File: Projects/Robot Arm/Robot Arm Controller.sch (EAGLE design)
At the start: 64 parts, among them IC1 U_FTDICHIP_FT232RL, J1 ICSP HEADER, J2 SERVO PWR, J3 STEPPER, J4 J_MOLEX_502386, P1 P_USB_MINIUX60A-MB-5ST, P2 +12V INPUT, U1 UA78M05CDCY, U2 TPS71550DCKR, U3 U_ATMEGA328P-AU, U4 U_5VSWITCHER_TL2575-05IKTTR, U5 A4988ALT1, U6 U_OPAMP_MCP6001T-E/OT, Y1 CSTCE16M0V13

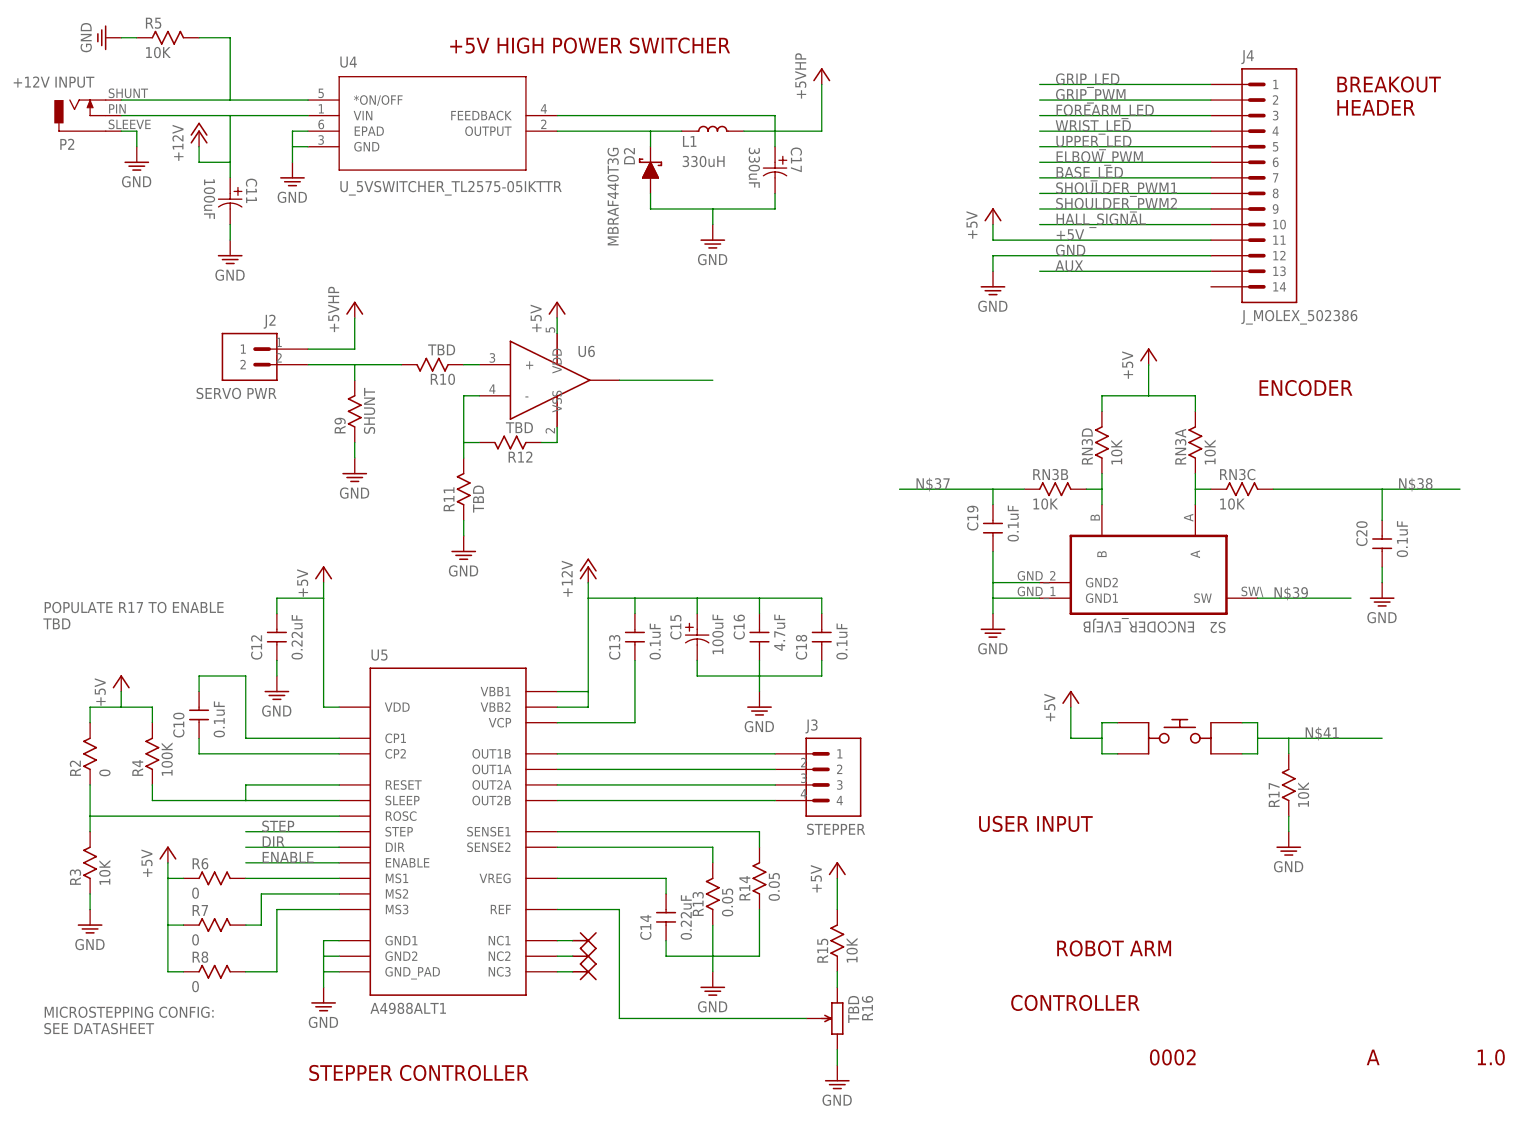
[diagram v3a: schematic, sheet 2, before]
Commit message: updated robot arm schematic to rev 1.1
- revisions to library
- 3A 5V support
- changed i/o position
- added component values
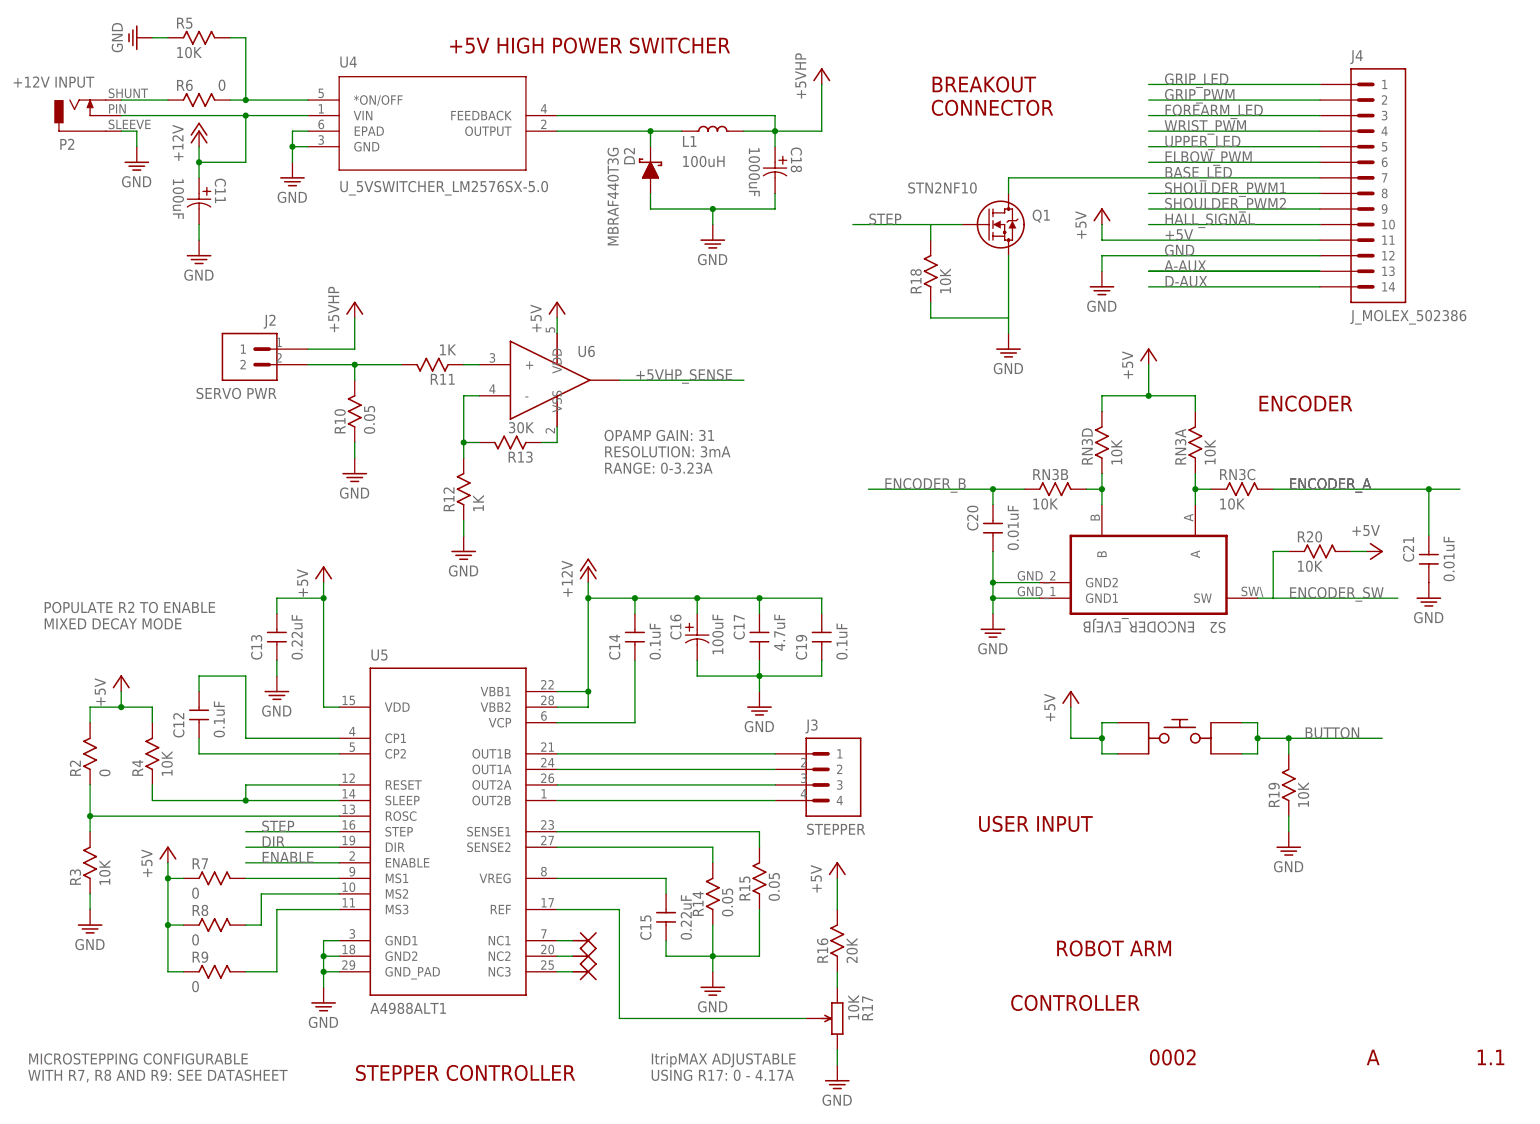
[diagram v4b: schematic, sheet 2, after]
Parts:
- added C21: 0.01uF, devon:C_CAPACITORC0805
- added Q1: STN2NF10, devon:Q_MOSFET_STN2NF10
- added R18, R19, R20: 10K, devon:R_RESISTOR0805
- C10: value 0.1uF -> 4.7uF
- C12, C14: value 0.22uF -> 0.1uF
- C13: value 0.1uF -> 0.22uF
- C15: value 100uF -> 0.22uF; device devon:C_CAPACITOR_ALUMINUM_PCAP_SVP_F12 -> devon:C_CAPACITORC0805
- C16: value 4.7uF -> 100uF; device devon:C_CAPACITORC1206 -> devon:C_CAPACITOR_ALUMINUM_PCAP_SVP_F12
- C17: value 330uF -> 4.7uF; device devon:C_CAPACITOR_ALUMINUM_PCAP_SVP_F12 -> devon:C_CAPACITORC1206
- C18: value 0.1uF -> 1000uF; device devon:C_CAPACITORC0805 -> devon:C_CAPACITOR_ALUMINUM_PCAP_SVP_F12
- C20: value 0.1uF -> 0.01uF
- C9: value 4.7uF -> 0.1uF
- L1: value 330uH -> 100uH; device devon:L_INDUCTOR_CLF12577NI-D -> devon:L_INDUCTOR_PA4344.104NLT
- R10: value TBD -> 0.05; device devon:R_RESISTOR0805 -> devon:R_RESISTOR1206
- R11, R12: value TBD -> 1K
- R13: value 0.05 -> 30K; device devon:R_RESISTOR1206 -> devon:R_RESISTOR0805
- R15: value 10K -> 0.05; device devon:R_RESISTOR0805 -> devon:R_RESISTOR1206
- R16: value TBD -> 20K; device devon:R_POT_EVM-2WSX80B14 -> devon:R_RESISTOR0805
- R17: device devon:R_RESISTOR0805 -> devon:R_POT_EVM-2WSX80B14
- R4: value 100K -> 10K
- R9: value SHUNT -> 0; device devon:R_RESISTOR1206 -> devon:R_RESISTOR0805
- RN2: value 10K -> 1K
- U4: value U_5VSWITCHER_TL2575-05IKTTR -> U_5VSWITCHER_LM2576SX-5.0; device devon:U_5VSWITCHER_TL2575-05IKTTR -> devon:U_5VSWITCHER_LM2576SX-5.0/NOPB
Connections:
- removed net A0: U3.PC0(ADC0)
- removed net A1: U3.PC1(ADC1)
- removed net A2: U3.PC2(ADC2)
- removed net A3: U3.PC3(ADC3)
- removed net A4: U3.PC4(ADC4)
- removed net A5: U3.PC5(ADC5)
- removed net A6: U3.ADC6
- removed net A7: U3.ADC7
- removed net AUX: J4.13
- removed net D10: U3.PB2
- removed net D2: U3.PD2
- removed net D3: U3.PD3
- removed net D4: U3.PD4
- removed net D5: U3.PD5
- removed net D6: U3.PD6
- removed net D7: U3.PD7
- removed net D8: U3.PB0
- removed net D9: U3.PB1
- removed net N$37: C19.2, RN3B.1
- removed net N$38: C20.2, RN3C.2
- removed net N$39: S2.SW
- removed net N$41: R17.2, S3.3, S3.4
- removed net N$49: U6.VOUT
- removed net WRIST_LED: J4.4
- new net +5VHP_SENSE: U3.ADC6, U6.VOUT
- new net A-AUX: J4.13, U3.ADC7
- new net BUTTON: R19.2, S3.3, S3.4, U3.PC3(ADC3)
- new net D-AUX: J4.14, U3.PC0(ADC0)
- new net ENCODER_A: C21.2, RN3C.2, U3.PD2(D2)
- new net ENCODER_B: C20.2, RN3B.1, U3.PC5(ADC5)
- new net ENCODER_SW: R20.1, S2.SW, U3.PC4(ADC4)
- new net N$66: P1.2
- new net N$67: P2.SHUNT, R6.1
- new net STAT: RN1A.2, U3.PB5(D13)
- new net WRIST_PWM: J4.4, U3.PB2(D10)
- net +12V: now also C14.1, C16.11, C17.2, C19.1; no longer C13.1, C15.11, C16.2, C18.1
- net +5V: now also C10.1, C13.1, C18.11, C7.1, LED3.A, LED4.A, R16.2, R20.2, R9.1; no longer C12.1, C17.11, C6.1, C9.1, LED3.C, LED4.C, R15.2, R6.1
- net BASE_LED: now also Q1.2
- net D11/MOSI: no longer U3.PB3
- net D12/MISO: no longer U3.PB4
- net D13/SCK: no longer RN1A.2, U3.PB5
- net DIR: now also U3.PD3(D3)
- net ELBOW_PWM: now also U3.PB1(D9)
- net ENABLE: now also U3.PC2(ADC2)
- net FOREARM_LED: now also U3.PB0(D8)
- net GND: now also C10.2, C13.2, C15.2, C16.22, C17.1, C18.22, C19.2, C21.1, C8.2, Q1.3, R10.1, R12.1, R15.1, R17.3, R18.1, R19.1; no longer C12.2, C14.2, C15.22, C16.1, C17.22, C18.2, C19.1, C9.2, R11.1, R13.1, R16.3, R17.1, R9.1
- net GRIP_LED: now also U3.PB4(D12)
- net GRIP_PWM: now also U3.PB3(D11)
- net HALL_SIGNAL: now also U3.PC1(ADC1)
- net N$11: now also C6.1
- net N$20: now also U3.PD0(RX); no longer U3.PD0
- net N$27: now also C9.2; no longer C8.2
- net N$30: now also LED3.C; no longer LED3.A
- net N$31: now also LED4.C; no longer LED4.A
- net N$35: now also R6.2; no longer P2.SHUNT
- net N$42: now also R13.1; no longer R12.1
- net N$43: now also R11.1; no longer R10.1
- net N$44: now also R13.2; no longer R11.2
- net N$45: now also R11.2; no longer R9.2
- net N$50: now also C15.1; no longer C14.1
- net N$51: now also R14.2; no longer R13.2
- net N$52: now also R17.1; no longer R15.1
- net N$53: now also R15.2; no longer R14.2
- net N$54: now also R17.2; no longer R16.2
- net N$58: now also C14.2; no longer C13.2
- net N$59: now also C12.2; no longer C10.2
- net N$6: now also C8.1; no longer C7.1
- net N$60: now also C12.1; no longer C10.1
- net N$61: now also R8.2; no longer R7.2
- net N$62: now also R7.2; no longer R6.2
- net N$63: now also R9.2; no longer R8.2
- net N$9: now also U3.PD1(TX); no longer U3.PD1
- net RESET: now also C9.1; no longer C8.1
- net SHOULDER_PWM1: now also U3.PD5(D5)
- net SHOULDER_PWM2: now also U3.PD6(D6)
- net STEP: now also Q1.1, R18.2, U3.PD4(D4)
- net UPPER_LED: now also U3.PD7(D7)
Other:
- note added: "1.1"
- note added: "BREAKOUT CONNECTOR"
- note added: "ItripMAX ADJUSTABLE USING R17: 0 - 4.17A"
- note added: "MICROSTEPPING CONFIGURABLE WITH R7, R8 AND R9: SEE DATASHEET"
- note added: "OPAMP GAIN: 31 RESOLUTION: 3mA RANGE: 0-3.23A"
- note added: "POPULATE R2 TO ENABLE MIXED DECAY MODE"
- note removed: "1.0"
- note removed: "BREAKOUT HEADER"
- note removed: "MICROSTEPPING CONFIG: SEE DATASHEET"
- note removed: "POPULATE R17 TO ENABLE TBD"
- moved on the sheet: C11, C12, C13, C14, C19, C20, C4, C6, C7, C8, C9, J4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

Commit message: Started placing components
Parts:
- added C22: 0.1uF, devon:C_CAPACITORC0805
- C11, C16: device devon:C_CAPACITOR_ALUMINUM_PCAP_SVP_F12 -> devon:C_100UF_ALUMINUM_APXG160ARA101ME61G
- C18: device devon:C_CAPACITOR_ALUMINUM_PCAP_SVP_F12 -> devon:C_1000UF_ALUMINUM_APXG160ARA102MJA0G
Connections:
- net A-AUX renamed A_AUX
- net D-AUX renamed D_AUX
- net +12V: now also C11.+, C16.+, C22.1; no longer C11.11, C16.11
- net +5V: now also C18.+; no longer C18.11
- net GND: now also C11.-, C16.-, C18.-, C22.2; no longer C11.22, C16.22, C18.22
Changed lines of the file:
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@@
 <part name="ZZ17" library="devon" deviceset="ZZ_NC" device=""/>
 <part name="U4" library="devon" deviceset="U_5VSWITCHER_LM2576SX-5.0/NOPB" device="" value="U_5VSWITCHER_LM2576SX-5.0"/>
-<part name="C11" library="devon" deviceset="C_CAPACITOR_ALUMINUM_PCAP_SVP_F12" device="" value="100uF"/>
-<part name="C18" library="devon" deviceset="C_CAPACITOR_ALUMINUM_PCAP_SVP_F12" device="" value="1000uF"/>
+<part name="C11" library="devon" deviceset="C_100UF_ALUMINUM_APXG160ARA101ME61G" device="" value="100uF"/>
+<part name="C18" library="devon" deviceset="C_1000UF_ALUMINUM_APXG160ARA102MJA0G" device="" value="1000uF"/>
 <part name="L1" library="devon" deviceset="L_INDUCTOR_PA4344.104NLT" device="" value="100uH"/>
 <part name="P2" library="devon" deviceset="P_BARREL_2.1MM" device="" value="+12V INPUT"/>
@@
 <part name="R14" library="devon" deviceset="R_RESISTOR" device="1206" value="0.05"/>
 <part name="R15" library="devon" deviceset="R_RESISTOR" device="1206" value="0.05"/>
-<part name="C16" library="devon" deviceset="C_CAPACITOR_ALUMINUM_PCAP_SVP_F12" device="" value="100uF"/>
+<part name="C16" library="devon" deviceset="C_100UF_ALUMINUM_APXG160ARA101ME61G" device="" value="100uF"/>
 <part name="C17" library="devon" deviceset="C_CAPACITOR" device="C1206" value="4.7uF"/>
 <part name="C15" library="devon" deviceset="C_CAPACITOR" device="C0805" value="0.22uF"/>
@@
 <part name="R20" library="devon" deviceset="R_RESISTOR" device="0805" value="10K"/>
 <part name="P+24" library="devon-supply" deviceset="+5V" device=""/>
+<part name="C22" library="devon" deviceset="C_CAPACITOR" device="C0805" value="0.1uF"/>
 </parts>
 <sheets>
@@
 <segment>
 <pinref part="U3" gate="A" pin="ADC6"/>
-<wire x1="142.24" y1="-40.64" x2="127" y2="-40.64" width="0.1524" layer="91"/>
-<label x="129.54" y="-40.64" size="1.778" layer="95"/>
-</segment>
-</net>
-<net name="A-AUX" class="0">
-<segment>
-<pinref part="U3" gate="A" pin="ADC7"/>
-<wire x1="142.24" y1="-43.18" x2="127" y2="-43.18" width="0.1524" layer="91"/>
-<label x="129.54" y="-43.18" size="1.778" layer="95"/>
+<wire x1="142.24" y1="-40.64" x2="119.38" y2="-40.64" width="0.1524" layer="91"/>
+<label x="121.92" y="-40.64" size="1.778" layer="95"/>
 </segment>
 </net>
@@
 </segment>
 </net>
-<net name="D-AUX" class="0">
-<segment>
-<pinref part="U3" gate="A" pin="PC0(ADC0)"/>
-<wire x1="185.42" y1="-30.48" x2="200.66" y2="-30.48" width="0.1524" layer="91"/>
-<label x="187.96" y="-30.48" size="1.778" layer="95"/>
-</segment>
-</net>
 <net name="HALL_SIGNAL" class="0">
 <segment>
@@
 <wire x1="142.24" y1="-63.5" x2="119.38" y2="-63.5" width="0.1524" layer="91"/>
 <label x="121.92" y="-63.5" size="1.778" layer="95"/>
+</segment>
+</net>
+<net name="A_AUX" class="0">
+<segment>
+<pinref part="U3" gate="A" pin="ADC7"/>
+<wire x1="142.24" y1="-43.18" x2="119.38" y2="-43.18" width="0.1524" layer="91"/>
+<label x="121.92" y="-43.18" size="1.778" layer="95"/>
+</segment>
+</net>
+<net name="D_AUX" class="0">
+<segment>
+<pinref part="U3" gate="A" pin="PC0(ADC0)"/>
+<wire x1="185.42" y1="-30.48" x2="200.66" y2="-30.48" width="0.1524" layer="91"/>
+<label x="187.96" y="-30.48" size="1.778" layer="95"/>
 </segment>
 </net>
@@
 <instance part="R20" gate="A" x="215.9" y="-91.44"/>
 <instance part="P+24" gate="1" x="226.06" y="-91.44" rot="R270"/>
+<instance part="C22" gate="G$1" x="144.78" y="-109.22" rot="R90"/>
 </instances>
 <busses>
@@
 </segment>
 <segment>
-<pinref part="C11" gate="A" pin="22"/>
+<pinref part="C11" gate="A" pin="-"/>
 <wire x1="33.02" y1="-38.1" x2="33.02" y2="-40.64" width="0.1524" layer="91"/>
 <pinref part="GND19" gate="1" pin="GND"/>
@@
 <pinref part="D2" gate="G$1" pin="A"/>
 <wire x1="106.68" y1="-33.02" x2="106.68" y2="-35.56" width="0.1524" layer="91"/>
-<pinref part="C18" gate="A" pin="22"/>
+<pinref part="C18" gate="A" pin="-"/>
 <wire x1="106.68" y1="-35.56" x2="116.84" y2="-35.56" width="0.1524" layer="91"/>
 <wire x1="116.84" y1="-35.56" x2="127" y2="-35.56" width="0.1524" layer="91"/>
@@
 <wire x1="134.62" y1="-111.76" x2="124.46" y2="-111.76" width="0.1524" layer="91"/>
 <wire x1="124.46" y1="-111.76" x2="124.46" y2="-109.22" width="0.1524" layer="91"/>
-<pinref part="C16" gate="A" pin="22"/>
+<pinref part="C16" gate="A" pin="-"/>
 <wire x1="124.46" y1="-111.76" x2="114.3" y2="-111.76" width="0.1524" layer="91"/>
 <wire x1="114.3" y1="-111.76" x2="114.3" y2="-109.22" width="0.1524" layer="91"/>
@@
 <pinref part="GND27" gate="1" pin="GND"/>
 <junction x="124.46" y="-111.76"/>
+<pinref part="C22" gate="G$1" pin="2"/>
+<wire x1="144.78" y1="-109.22" x2="144.78" y2="-111.76" width="0.1524" layer="91"/>
+<wire x1="144.78" y1="-111.76" x2="134.62" y2="-111.76" width="0.1524" layer="91"/>
+<junction x="134.62" y="-111.76"/>
 </segment>
 <segment>
@@
 <wire x1="40.64" y1="-27.94" x2="40.64" y2="-20.32" width="0.1524" layer="91"/>
 <wire x1="33.02" y1="-27.94" x2="40.64" y2="-27.94" width="0.1524" layer="91"/>
-<pinref part="C11" gate="A" pin="11"/>
+<pinref part="C11" gate="A" pin="+"/>
 <wire x1="33.02" y1="-27.94" x2="33.02" y2="-30.48" width="0.1524" layer="91"/>
 <junction x="40.64" y="-20.32"/>
@@
 <wire x1="114.3" y1="-99.06" x2="124.46" y2="-99.06" width="0.1524" layer="91"/>
 <wire x1="124.46" y1="-99.06" x2="124.46" y2="-101.6" width="0.1524" layer="91"/>
-<pinref part="C16" gate="A" pin="11"/>
+<pinref part="C16" gate="A" pin="+"/>
 <pinref part="C17" gate="G$1" pin="2"/>
 <pinref part="C19" gate="G$1" pin="1"/>
 <wire x1="124.46" y1="-99.06" x2="134.62" y2="-99.06" width="0.1524" layer="91"/>
-<wire x1="134.62" y1="-99.06" x2="134.62" y2="-101.6" width="0.1524" layer="91"/>
 <junction x="104.14" y="-99.06"/>
 <junction x="114.3" y="-99.06"/>
@@
 <junction x="96.52" y="-99.06"/>
 <junction x="96.52" y="-114.3"/>
+<wire x1="134.62" y1="-99.06" x2="134.62" y2="-101.6" width="0.1524" layer="91"/>
+<pinref part="C22" gate="G$1" pin="1"/>
+<wire x1="134.62" y1="-99.06" x2="144.78" y2="-99.06" width="0.1524" layer="91"/>
+<wire x1="144.78" y1="-99.06" x2="144.78" y2="-101.6" width="0.1524" layer="91"/>
+<junction x="134.62" y="-99.06"/>
 </segment>
 </net>
@@
 <pinref part="L1" gate="A" pin="2"/>
 <wire x1="121.92" y1="-22.86" x2="127" y2="-22.86" width="0.1524" layer="91"/>
-<pinref part="C18" gate="A" pin="11"/>
+<pinref part="C18" gate="A" pin="+"/>
 <wire x1="127" y1="-22.86" x2="134.62" y2="-22.86" width="0.1524" layer="91"/>
 <wire x1="127" y1="-25.4" x2="127" y2="-22.86" width="0.1524" layer="91"/>
@@
 </segment>
 </net>
-<net name="A-AUX" class="0">
+<net name="A_AUX" class="0">
 <segment>
 <pinref part="J4" gate="A" pin="13"/>
@@
 </segment>
 </net>
-<net name="D-AUX" class="0">
+<net name="D_AUX" class="0">
 <segment>
 <pinref part="J4" gate="A" pin="14"/>
